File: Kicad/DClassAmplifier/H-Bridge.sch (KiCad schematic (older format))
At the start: 16 parts, among them Q1 PHP23NQ11T,127, Q2 PHP23NQ11T,127, Q3 PHP23NQ11T,127, Q4 PHP23NQ11T,127, U2 DGD05463FN-7, U3 DGD05463FN-7

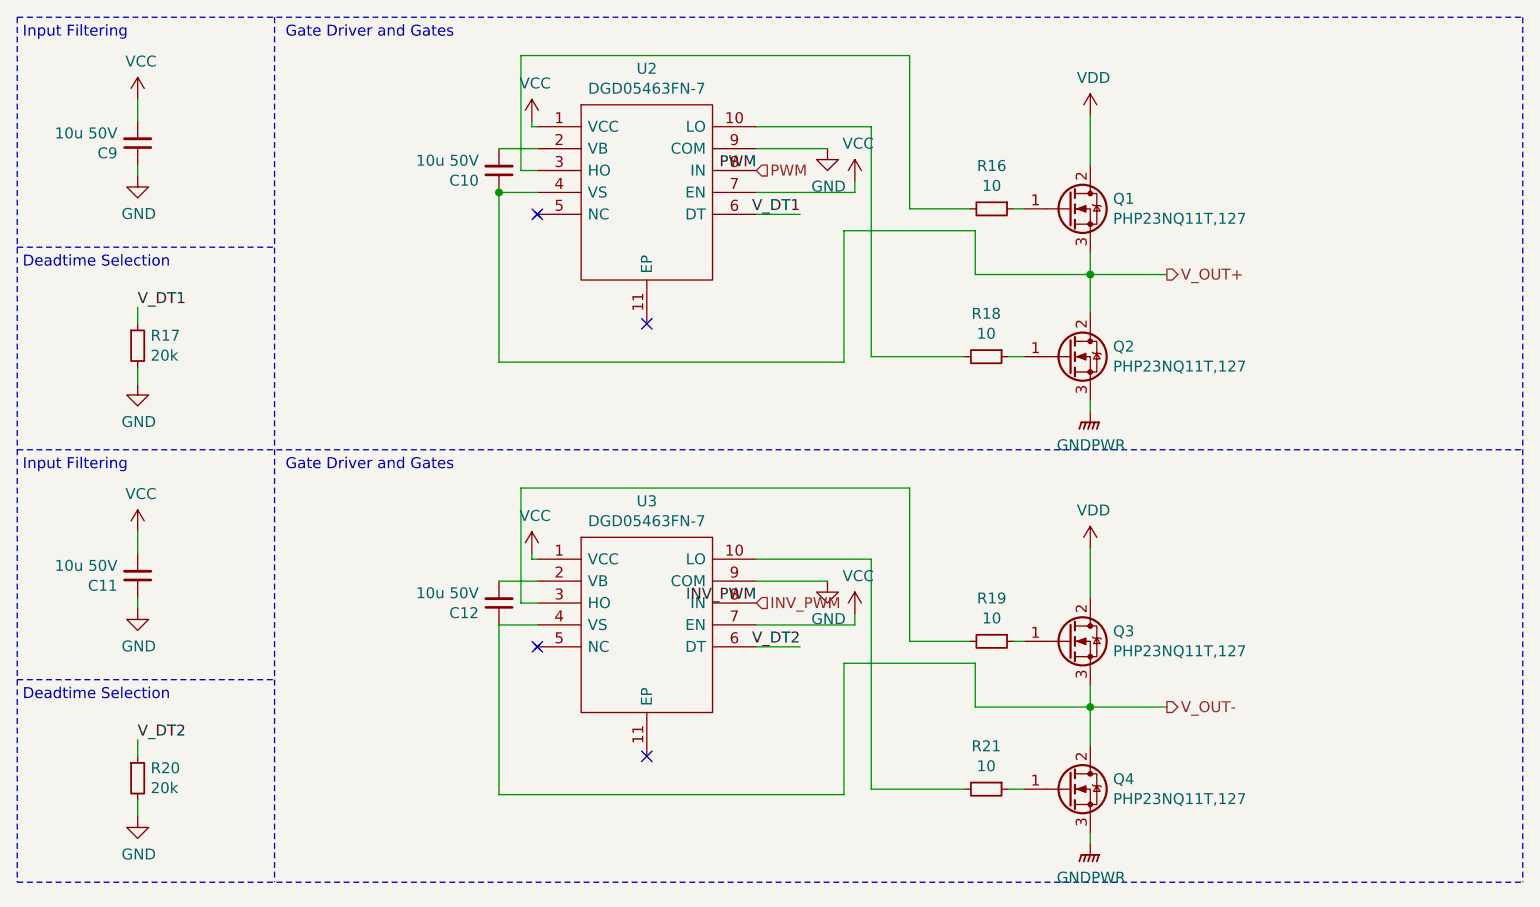
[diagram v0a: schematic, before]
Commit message: Add 10V Reg and Reroute
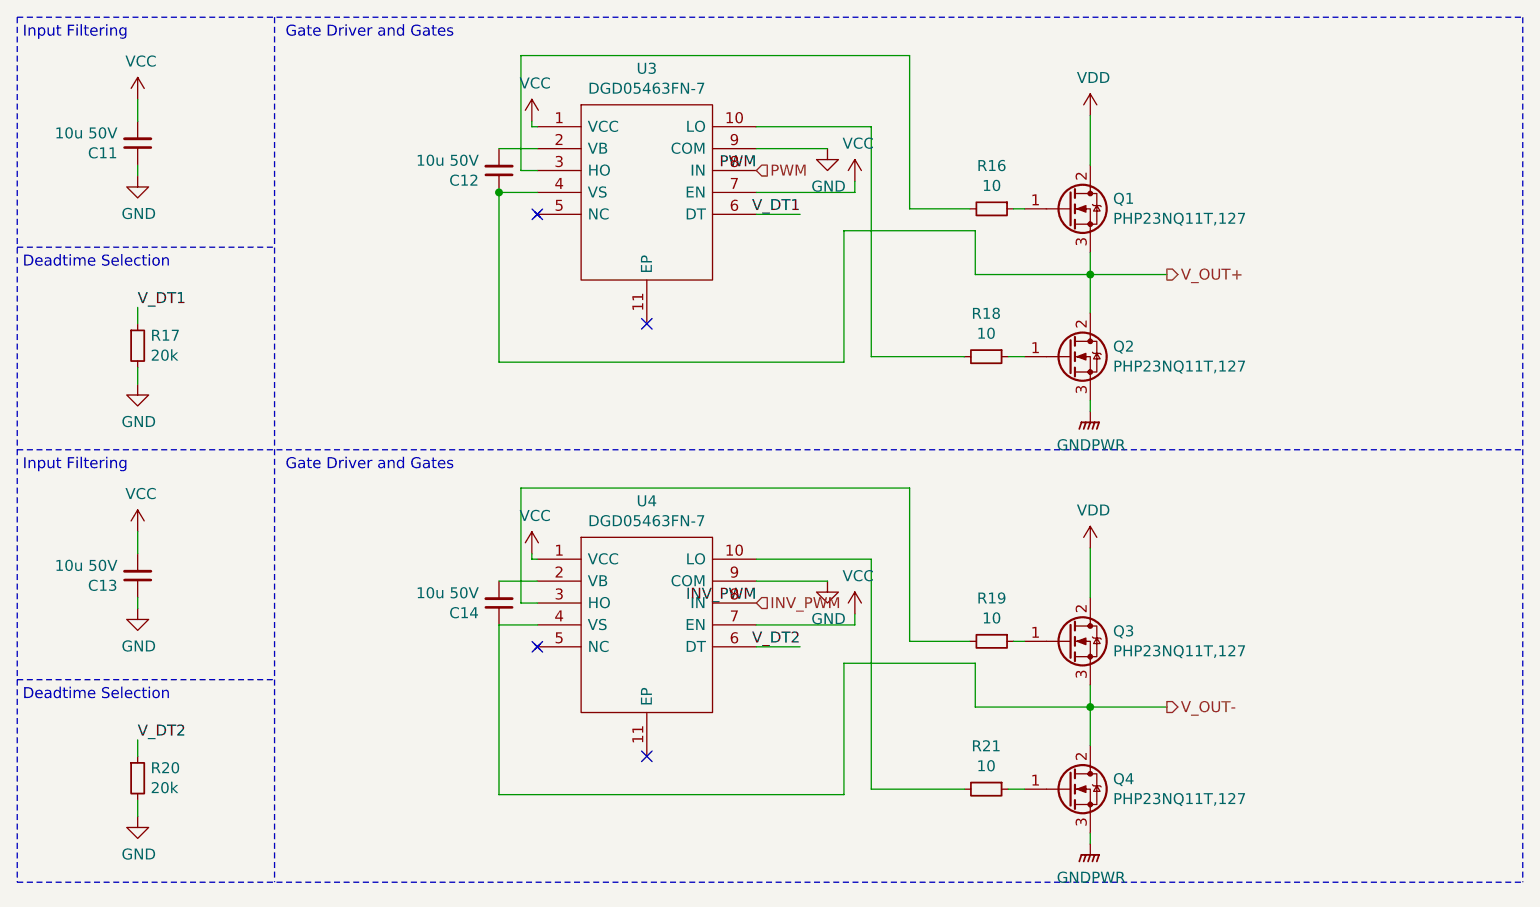
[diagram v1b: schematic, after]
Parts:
- renumbered C9 to C11, C10 to C12, C11 to C13, C12 to C14, U2 to U3, U3 to U4
